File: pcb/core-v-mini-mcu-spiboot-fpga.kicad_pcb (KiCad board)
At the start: 4 copper layers, 38.5 x 40 mm, 36 parts, among them J1 Conn_02x10_Odd_Even, P1 USB Micro, U1 93C46B, U2 FT4232H, U3 W25Q

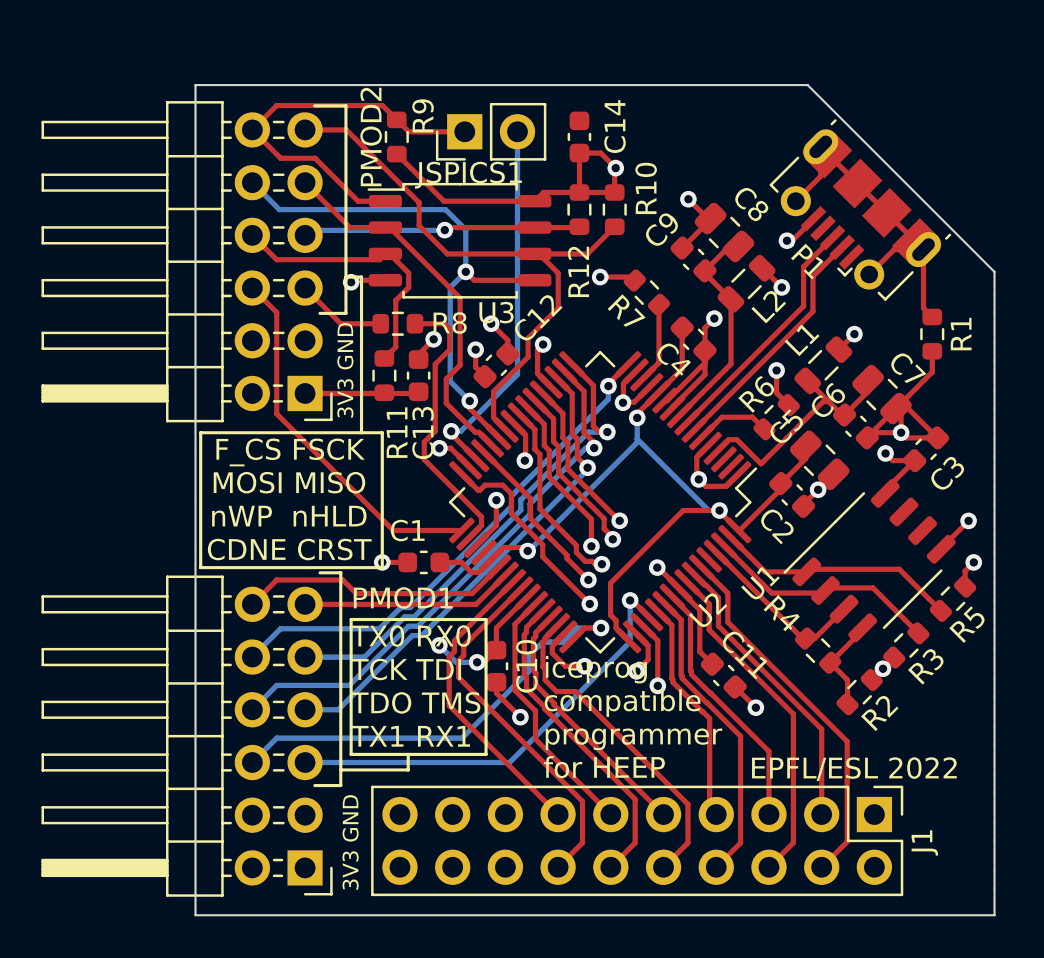
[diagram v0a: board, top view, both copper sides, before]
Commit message: Revision 2: Converted to the available 56 pin QFN package, added missing oscillator
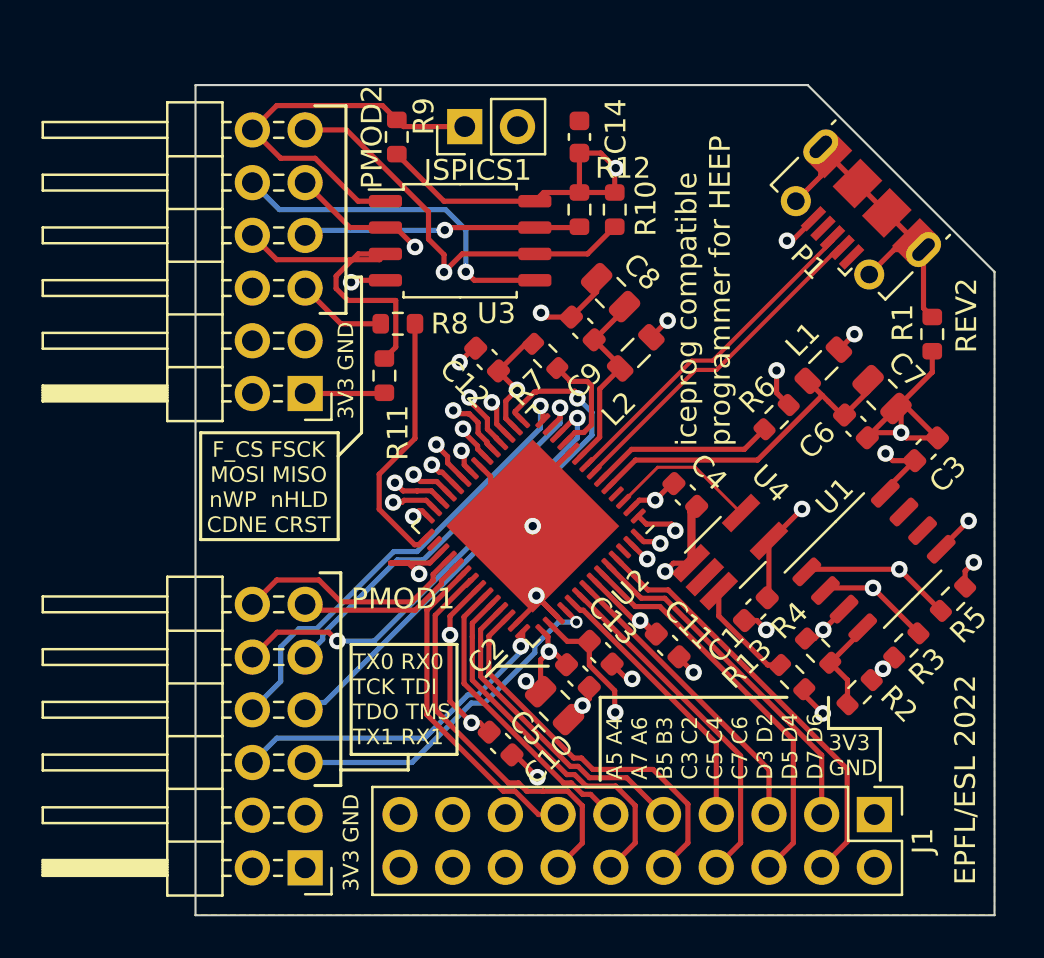
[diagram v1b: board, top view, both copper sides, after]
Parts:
- added R13: 10k, Resistor_SMD:R_0603_1608Metric, F.Cu at (104.8, 100.0)
- added U4: SIT2001BI-S2-33E-12.000000D, Package_TO_SOT_SMD:TSOT-23-5_HandSoldering, F.Cu at (101.8, 94.0)
- U2: value FT4232H -> FT4232H-56Q; footprint Package_QFP:LQFP-64_10x10mm_P0.5mm -> Package_DFN_QFN:QFN-56-1EP_8x8mm_P0.5mm_EP5.9x5.9mm
- moved C5 17.4 mm to (93.3, 101.4)
- moved C1 16.2 mm to (103.0, 96.8), turned to 45 degrees
- moved C13 16.0 mm to (95.5, 98.8), turned to -45 degrees
- moved C2 13.5 mm to (94.4, 100.0)
- moved C4 7.51 mm to (99.6, 91.2)
- moved C9 6.29 mm to (94.7, 83.2)
- moved L2 6.29 mm to (97.2, 84.4)
- moved C8 6.21 mm to (96.0, 81.5)
- moved R7 5.77 mm to (92.8, 84.5)
- moved C10 3.73 mm to (90.7, 103.2), turned to -45 degrees
- moved U2 3.45 mm to (92.2, 92.8)
- moved C11 3.07 mm to (98.8, 98.5)
- moved C12 0.53 mm to (90.0, 84.7), turned to 135 degrees
- moved JSPICS1 0.25 mm to (89.0, 73.5)
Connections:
- net /USBDM renamed /USB_D-
- net /USBDP renamed /USB_D+
- C1 pad 1: /VCORE -> GND
- C1 pad 2: GND -> +3V3
- U2 pad 1: GND -> /EECS
- U2 pad 11: GND -> Net-(R7-Pad1)
- U2 pad 12: /VCORE -> /TCK
- U2 pad 13: GND -> /TDI
- U2 pad 14: Net-(R7-Pad1) -> /TDO
- U2 pad 15: GND -> /TMS
- U2 pad 16: /TCK -> +3V3
- U2 pad 17: /TDI -> /A4
- U2 pad 18: /TDO -> /A5
- U2 pad 19: /TMS -> /A6
- U2 pad 2: /CK12MHZ -> /VCORE
- U2 pad 20: +3V3 -> /A7
- U2 pad 21: /A4 -> GND
- U2 pad 22: /A5 -> /FLASH_SCK
- U2 pad 23: /A6 -> /FLASH_MOSI
- U2 pad 24: /A7 -> /FLASH_MISO
- U2 pad 25: GND -> /SPI_CS
- U2 pad 26: /FLASH_SCK -> /iCE_SS_B
- U2 pad 27: /FLASH_MOSI -> /B5
- U2 pad 28: /FLASH_MISO -> /iCE_CDONE
- U2 pad 29: /SPI_CS -> Net-(R8-Pad1)
- U2 pad 3: unconnected-(U2-Pad3) -> /CK12MHZ
- U2 pad 30: /iCE_SS_B -> unconnected-(U2-Pad30)
- U2 pad 31: +3V3 -> /VCORE
- U2 pad 32: /B5 -> /TX0
- U2 pad 33: /iCE_CDONE -> /RX0
- U2 pad 34: Net-(R8-Pad1) -> /C2
- U2 pad 35: GND -> /C3
- U2 pad 36: unconnected-(U2-Pad36) -> +3V3
- U2 pad 37: /VCORE -> /C4
- U2 pad 38: /TX0 -> /C5
- U2 pad 39: /RX0 -> /C6
- U2 pad 4: Net-(C6-Pad1) -> unconnected-(U2-Pad4)
- U2 pad 40: /C2 -> /C7
- U2 pad 41: /C3 -> GND
- U2 pad 42: +3V3 -> /TX1
- U2 pad 43: /C4 -> /VCORE
- U2 pad 44: /C5 -> +3V3
- U2 pad 45: /C6 -> GND
- U2 pad 46: /C7 -> /RX1
- U2 pad 47: GND -> /D2
- U2 pad 48: /TX1 -> /D3
- U2 pad 49: /VCORE -> /D4
- U2 pad 5: GND -> Net-(C6-Pad1)
- U2 pad 51: GND -> /D5
- U2 pad 52: /RX1 -> /D6
- U2 pad 53: /D2 -> /D7
- U2 pad 54: /D3 -> unconnected-(U2-Pad54)
- U2 pad 55: /D4 -> Net-(R4-Pad1)
- U2 pad 56: +3V3 -> Net-(R3-Pad1)
- U2 pad 57: /D5 -> GND
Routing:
- net /VCORE: track 40.8 -> 12.0 mm, vias 3 -> 4
- net /EECS: track 11.7 -> 21.1 mm, vias 0 -> 2
- net /CK12MHZ: track 0.00 -> 7.25 mm
- net Net-(R3-Pad1): track 11.3 -> 17.8 mm, vias 0 -> 2
- net /TX1: track 21.6 -> 16.2 mm
- net Net-(R4-Pad1): track 8.45 -> 13.7 mm, vias 0 -> 2
- net Net-(R6-Pad2): track 3.66 -> 8.85 mm
- net Net-(R13-Pad1): track 0.00 -> 5.13 mm
- net Net-(C6-Pad1): track 11.9 -> 16.7 mm
- net /USB_D-: track 11.7 -> 16.4 mm
- net /USB_D+: track 11.8 -> 16.4 mm
- net /TDI: track 23.6 -> 19.0 mm
- net /RX1: track 21.4 -> 16.9 mm
- net /iCE_SS_B: track 17.9 -> 22.4 mm
- net /FLASH_MOSI: track 26.0 -> 30.2 mm
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- added copper zone on In2.Cu, net +3V3
- added copper zone on In2.Cu, net /VCORE
- added copper zone on In1.Cu, net GND
- removed copper zone on In1.Cu, net +3V3
- removed copper zone on In2.Cu, net GND
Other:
- board text added: "A5 A4 A7 A6 B5 B3 C3 C2 C5 C4 C7 C6 D3 D2 D5 D4 D7 D6"
- board text added: "REV2"

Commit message: QFN version
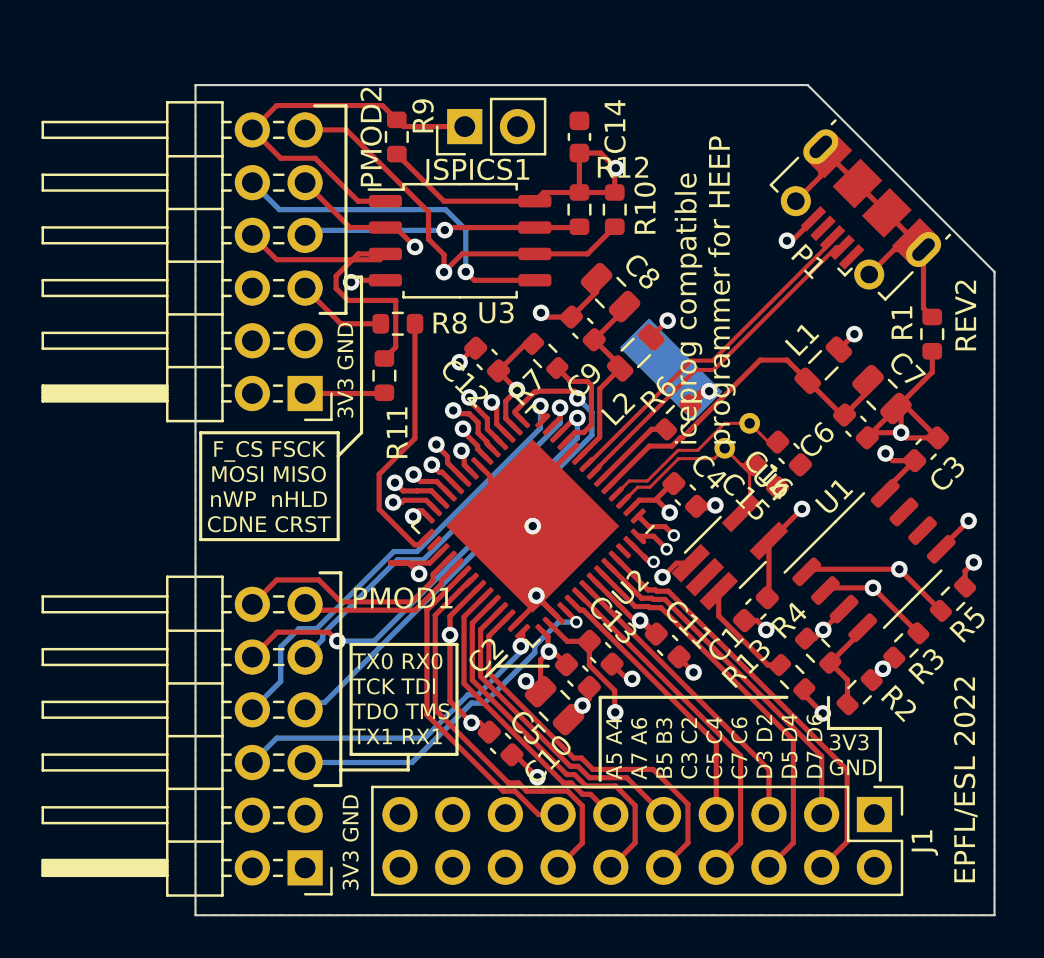
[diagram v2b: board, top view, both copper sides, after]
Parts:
- added C15: 30p, Capacitor_SMD:C_0603_1608Metric, F.Cu at (103.5, 90.3)
- added C16: 30p, Capacitor_SMD:C_0603_1608Metric, F.Cu at (104.6, 89.2)
- added Y1: Crystal_GND3, Crystal:Crystal_DS15_D1.5mm_L5.0mm_Horizontal_1EP_style1, B.Cu at (101.5, 89.0)
- moved R6 4.75 mm to (99.2, 87.5)
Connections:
- net Net-(R3-Pad1) renamed /EECLK
- net Net-(R4-Pad1) renamed /EEDAT
- U2 pad 4: unconnected-(U2-Pad4) -> /CK12MHZ_O
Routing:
- net /CK12MHZ_O: track 0.00 -> 9.57 mm
- net Net-(R6-Pad2): track 8.85 -> 4.10 mm
- net /CK12MHZ: track 7.25 -> 10.4 mm
- net GND: track 56.5 -> 54.2 mm, vias 15 -> 16
- net /VCORE: track 12.0 -> 13.0 mm

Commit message: QFN version
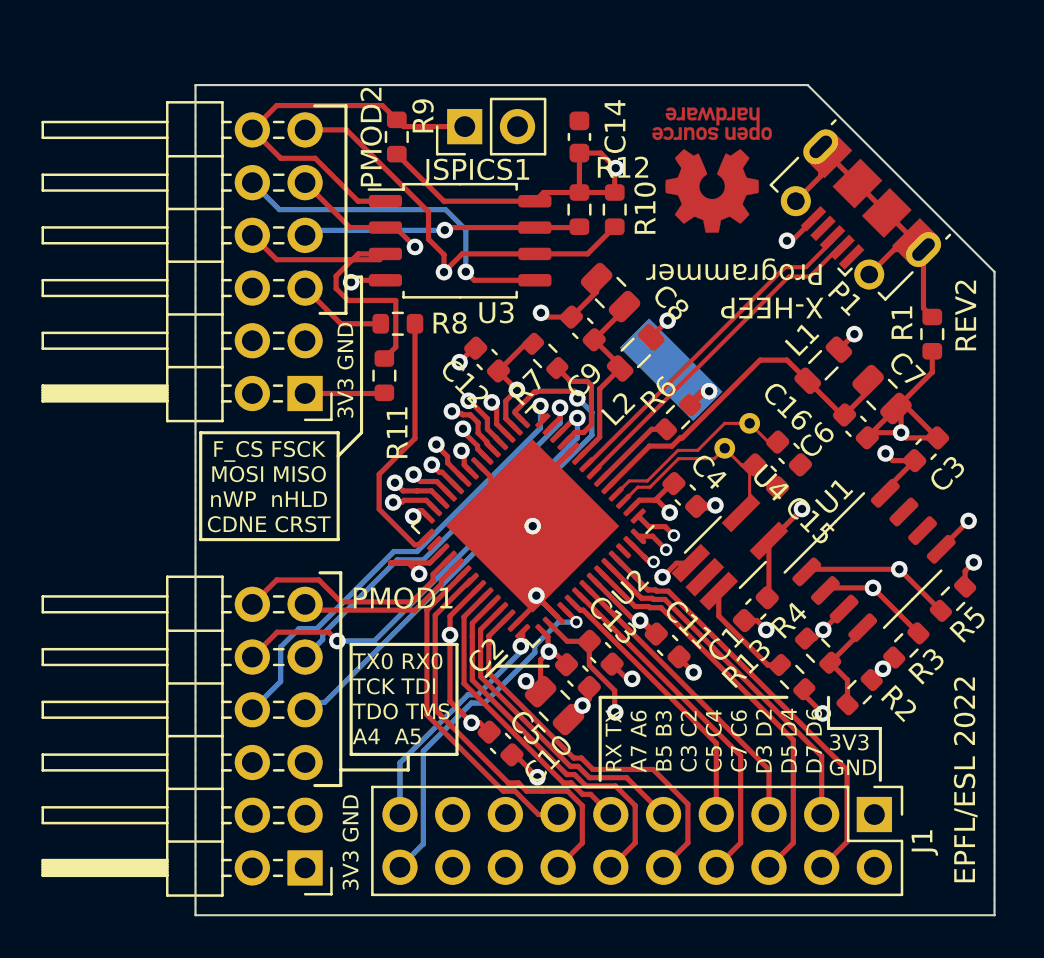
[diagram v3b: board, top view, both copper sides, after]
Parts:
- added REF**: OSHW-Logo_5.7x6mm_Copper, Symbol:OSHW-Logo_5.7x6mm_Copper, F.Cu at (100.9, 75.6)
- L1, L2: value 600 -> 600n
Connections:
- J1 pad 19: /A4 -> /TX1
- J1 pad 20: /A5 -> /RX1
- PMOD1 pad 5: /RX1 -> /A5
- PMOD1 pad 6: /TX1 -> /A4
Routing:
- net /A5: track 32.0 -> 25.8 mm
- net /TX1: track 16.2 -> 11.5 mm
- net /A4: track 30.1 -> 29.2 mm
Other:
- board text added: "RX TX A7 A6 B5 B3 C3 C2 C5 C4 C7 C6 D3 D2 D5 D4 D7 D6"
- board text added: "TX0 RX0 TCK TDI TDO TMS A4 A5"
- board text added: "X-HEEP Programmer"
- board text removed: "A5 A4 A7 A6 B5 B3 C3 C2 C5 C4 C7 C6 D3 D2 D5 D4 D7 D6"
- board text removed: "TX0 RX0 TCK TDI TDO TMS TX1 RX1"
- board text removed: "iceprog compatible programmer for HEEP"

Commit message: Programmer reverted to LQFP package, production files for JLCPCB order added.
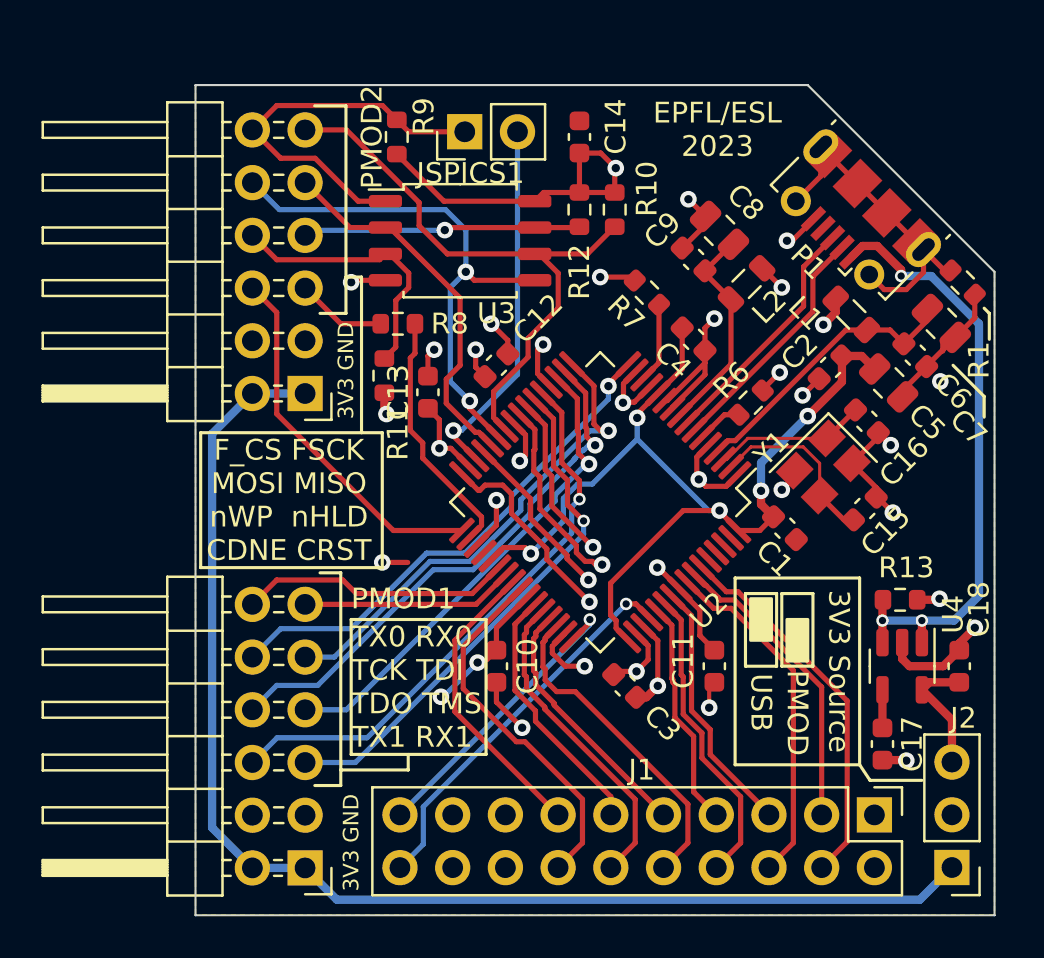
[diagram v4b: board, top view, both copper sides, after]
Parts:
- removed R2, R3, R5: 10k, Resistor_SMD:R_0603_1608Metric
- removed R4: 2k2, Resistor_SMD:R_0603_1608Metric
- removed REF**: OSHW-Logo_5.7x6mm_Copper, Symbol:OSHW-Logo_5.7x6mm_Copper
- removed U1: 93C46B, Package_SO:SSOP-8_3.9x5.05mm_P1.27mm
- added C17: 10n, Capacitor_SMD:C_0603_1608Metric, F.Cu at (109.1, 103.2)
- added C18: 10u, Capacitor_SMD:C_0603_1608Metric, F.Cu at (112.8, 99.5)
- added J2: Conn_01x03, Connector_PinHeader_2.54mm:PinHeader_1x03_P2.54mm_Vertical, F.Cu at (112.5, 109.2)
- U2: value FT4232H-56Q -> FT4232HL; footprint Package_DFN_QFN:QFN-56-1EP_8x8mm_P0.5mm_EP5.9x5.9mm -> Package_QFP:LQFP-64_10x10mm_P0.5mm
- U4: value SIT2001BI-S2-33E-12.000000D -> LP2985-3.3; footprint Package_TO_SOT_SMD:TSOT-23-5_HandSoldering -> Package_TO_SOT_SMD:SOT-23-5
- Y1: value Crystal_GND3 -> Crystal_GND24; footprint Crystal:Crystal_DS15_D1.5mm_L5.0mm_Horizontal_1EP_style1 -> Crystal:Crystal_SMD_3225-4Pin_3.2x2.5mm; moved to F.Cu
- moved C5 22.4 mm to (109.4, 85.8)
- moved C2 19.2 mm to (106.6, 85.1), turned to -135 degrees
- moved C3 18.4 mm to (96.7, 100.5), turned to -45 degrees
- moved C13 15.1 mm to (87.2, 86.3), turned to 90 degrees
- moved U4 9.96 mm to (110.0, 99.5), turned to -90 degrees
- moved C4 7.51 mm to (100.0, 83.8)
- moved R13 6.40 mm to (110.0, 96.3), turned to 0 degrees
- moved C9 6.29 mm to (100.0, 79.9)
- moved L2 6.29 mm to (102.6, 81.1)
- moved C8 6.05 mm to (101.2, 78.5)
- moved R7 5.77 mm to (97.8, 81.5)
- moved C15 5.00 mm to (108.2, 91.9), turned to -135 degrees
- moved Y1 4.83 mm to (106.2, 89.9), turned to -135 degrees
- moved C6 4.46 mm to (110.7, 84.5)
- moved C7 4.46 mm to (111.9, 83.0)
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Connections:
- C1 pad 1: GND -> /VCORE
- C1 pad 2: +3V3 -> GND
- P1 pad 1: /USB_5V -> +5V
- PMOD1 pad 1: +3V3 -> /3V3_PMOD
- PMOD1 pad 2: +3V3 -> /3V3_PMOD
- PMOD2 pad 1: +3V3 -> /3V3_PMOD
- PMOD2 pad 2: +3V3 -> /3V3_PMOD
- R13 pad 1: Net-(R13-Pad1) -> +5V
- R13 pad 2: +3V3 -> GND
- U2 pad 1: /EECS -> GND
- U2 pad 11: Net-(R7-Pad1) -> GND
- U2 pad 12: /TCK -> /VCORE
- U2 pad 13: /TDI -> GND
- U2 pad 14: /TDO -> Net-(R7-Pad1)
- U2 pad 15: /TMS -> GND
- U2 pad 16: +3V3 -> /TCK
- U2 pad 17: /A4 -> /TDI
- U2 pad 18: /A5 -> /TDO
- U2 pad 19: /A6 -> /TMS
- U2 pad 2: /VCORE -> /CK12MHZ
- U2 pad 20: /A7 -> +3V3
- U2 pad 21: GND -> /A4
- U2 pad 22: /FLASH_SCK -> /A5
- U2 pad 23: /FLASH_MOSI -> /A6
- U2 pad 24: /FLASH_MISO -> /A7
- U2 pad 25: /SPI_CS -> GND
- U2 pad 26: /iCE_SS_B -> /FLASH_SCK
- U2 pad 27: /B5 -> /FLASH_MOSI
- U2 pad 28: /iCE_CDONE -> /FLASH_MISO
- U2 pad 29: Net-(R8-Pad1) -> /SPI_CS
- U2 pad 3: /CK12MHZ -> /CK12MHZ_O
- U2 pad 30: unconnected-(U2-Pad30) -> /iCE_SS_B
- U2 pad 31: /VCORE -> +3V3
- U2 pad 32: /TX0 -> /B5
- U2 pad 33: /RX0 -> /iCE_CDONE
- U2 pad 34: /C2 -> Net-(R8-Pad1)
- U2 pad 35: /C3 -> GND
- U2 pad 36: +3V3 -> unconnected-(U2-Pad36)
- U2 pad 37: /C4 -> /VCORE
- U2 pad 38: /C5 -> /TX0
- U2 pad 39: /C6 -> /RX0
- U2 pad 4: /CK12MHZ_O -> Net-(C6-Pad1)
- U2 pad 40: /C7 -> /C2
- U2 pad 41: GND -> /C3
- U2 pad 42: /TX1 -> +3V3
- U2 pad 43: /VCORE -> /C4
- U2 pad 44: +3V3 -> /C5
- U2 pad 45: GND -> /C6
- U2 pad 46: /RX1 -> /C7
- U2 pad 47: /D2 -> GND
- U2 pad 48: /D3 -> /TX1
- U2 pad 49: /D4 -> /VCORE
- U2 pad 5: Net-(C6-Pad1) -> GND
- U2 pad 51: /D5 -> GND
- U2 pad 52: /D6 -> /RX1
- U2 pad 53: /D7 -> /D2
- U2 pad 54: unconnected-(U2-Pad54) -> /D3
- U2 pad 55: /EEDAT -> /D4
- U2 pad 56: /EECLK -> +3V3
- U2 pad 57: GND -> /D5
- U4 pad 1: GND -> +5V
- U4 pad 2: unconnected-(U4-Pad2) -> GND
- U4 pad 3: Net-(R13-Pad1) -> +5V
- U4 pad 4: +3V3 -> Net-(C17-Pad1)
- U4 pad 5: /CK12MHZ -> /3V3_LDO
- Y1 pad 1: /CK12MHZ -> /CK12MHZ_O
- Y1 pad 2: /CK12MHZ_O -> GND
- Y1 pad 3: GND -> /CK12MHZ
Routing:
- net /3V3_PMOD: track 0.00 -> 62.0 mm
- net /VCORE: track 13.0 -> 46.5 mm, vias 4 -> 5
- net +5V: track 0.00 -> 29.5 mm, vias 0 -> 3
- net /EECS: track 21.1 -> 0.00 mm, vias 2 -> 0
- net /EECLK: track 18.2 -> 0.00 mm, vias 2 -> 0
- net +3V3: track 61.5 -> 45.9 mm, vias 13 -> 12
- net /EEDAT: track 13.6 -> 0.00 mm, vias 2 -> 0
- net GND: track 54.2 -> 66.8 mm, vias 16 -> 24
- net /3V3_LDO: track 0.00 -> 6.03 mm
- net Net-(R13-Pad1): track 5.13 -> 0.00 mm
- net /USB_D-: track 16.4 -> 11.7 mm
- net Net-(R2-Pad1): track 4.68 -> 0.00 mm
- net /USB_D+: track 16.4 -> 11.8 mm
- net /iCE_SS_B: track 22.4 -> 17.8 mm
- net /TDI: track 19.0 -> 23.6 mm
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- added copper zone on In1.Cu, net +3V3
- added copper zone on In2.Cu, net GND
- removed copper zone on In2.Cu, net +3V3
- removed copper zone on In2.Cu, net /VCORE
- removed copper zone on In1.Cu, net GND
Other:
- board text added: "#"
- board text added: "3V3 Source"
- board text added: "EPFL / ESL 2023 V0.3"
- board text added: "EPFL/ESL 2023"
- board text added: "PMOD"
- board text added: "TX0 RX0 TCK TDI TDO TMS TX1 RX1"
- board text added: "USB"
- board text added: "iceprog compatible programmer for HEEP"
- board text removed: "EPFL/ESL 2022"
- board text removed: "REV2"
- board text removed: "RX TX A7 A6 B5 B3 C3 C2 C5 C4 C7 C6 D3 D2 D5 D4 D7 D6"
- board text removed: "TX0 RX0 TCK TDI TDO TMS A4 A5"
- board text removed: "X-HEEP Programmer"
